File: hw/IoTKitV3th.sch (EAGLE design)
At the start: 28 parts, among them J1 4P-2.0, J2 4P-2.0, J3 4P-2.0, J4 4p-2.54

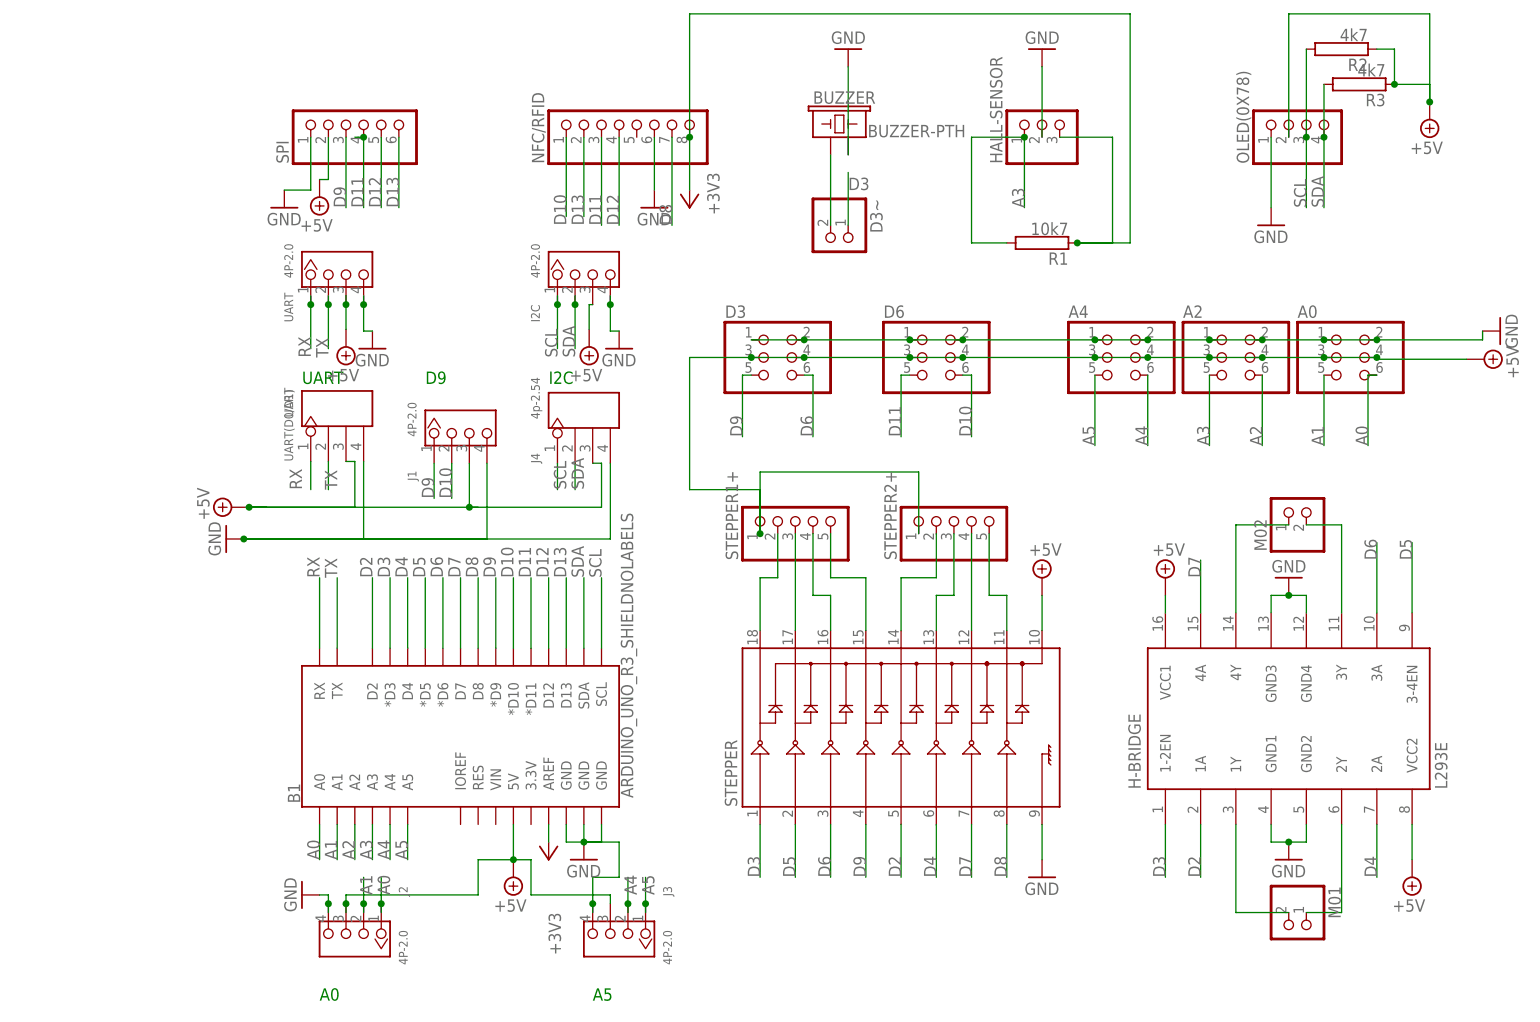
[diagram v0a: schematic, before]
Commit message: V1.1 inkl. SD Card, Poti, ESP8266, Schrift gekehrt
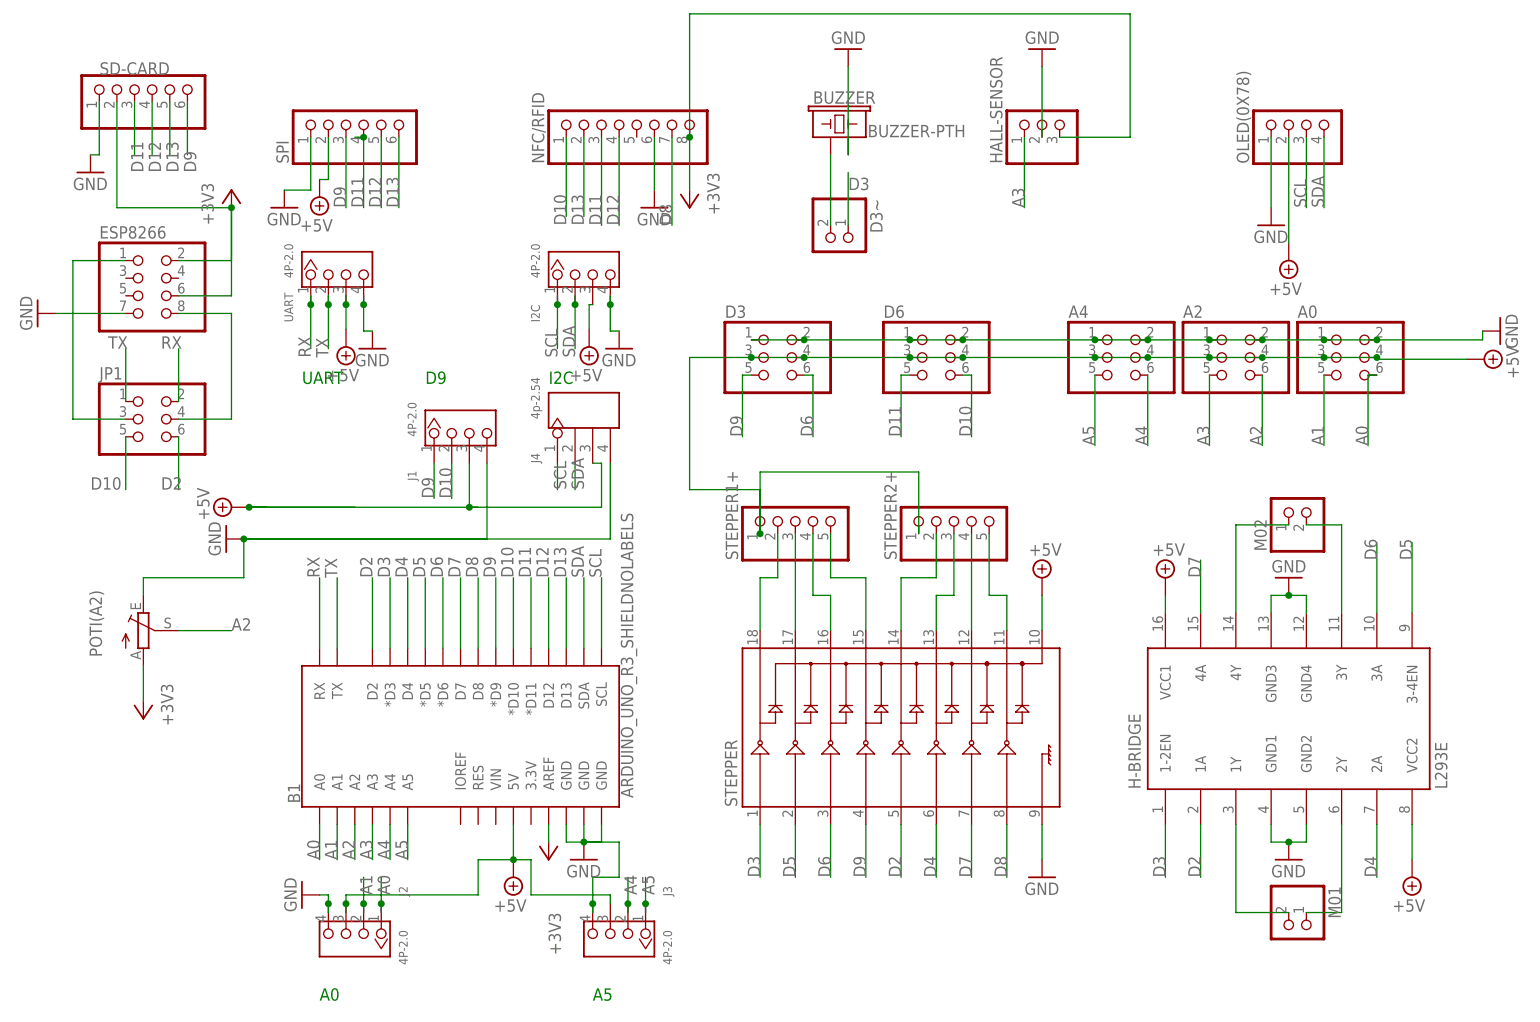
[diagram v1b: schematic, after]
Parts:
- removed R1: 10k7, resistor-power:RCA0001
- removed R2, R3: 4k7, resistor-power:RCA0001
- removed UART(D0/D1): UART, Seeed-Connector:DIP-BLACK-MALE-HEADER-VERT(4P-2.54)
- added ESP8266: (no value), pinhead:PINHD-2X4
- added JP1: (no value), pinhead:PINHD-2X3
- added POTI(A2): (no value), pot:TRIM_EU-B25P
- added SD-CARD: (no value), pinhead:PINHD-1X6
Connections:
- new net N$8: ESP8266.1, JP1.3
- new net N$9: ESP8266.8, JP1.4
- net +3V3: now also ESP8266.2, ESP8266.6, POTI(A2).A, SD-CARD.2; no longer R1.1
- net +5V: no longer R2.1, R3.1, UART(D0/D1).P$3
- net A2: now also POTI(A2).S
- net A3: no longer R1.2
- net D10: now also JP1.5
- net D11: now also SD-CARD.3
- net D12: now also SD-CARD.4
- net D13: now also SD-CARD.5
- net D2: now also JP1.6
- net D9: now also SD-CARD.6
- net GND: now also ESP8266.7, POTI(A2).E, SD-CARD.1; no longer UART(D0/D1).P$4
- net RX: now also JP1.2; no longer UART(D0/D1).P$1
- net SCL: no longer R2.2
- net SDA: no longer R3.2
- net TX: now also JP1.1; no longer UART(D0/D1).P$2

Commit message: Korrektur SD Karten belegung
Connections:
- net D11: now also SD-CARD.4; no longer SD-CARD.3
- net D12: now also SD-CARD.3; no longer SD-CARD.4
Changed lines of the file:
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@@
 </segment>
 <segment>
-<pinref part="SD-CARD" gate="A" pin="3"/>
-<wire x1="-21.59" y1="129.54" x2="-21.59" y2="121.92" width="0.1524" layer="91"/>
-<label x="-20.32" y="119.38" size="1.778" layer="95" rot="R90"/>
+<pinref part="SD-CARD" gate="A" pin="4"/>
+<wire x1="-19.05" y1="129.54" x2="-19.05" y2="121.92" width="0.1524" layer="91"/>
+<label x="-17.78" y="119.38" size="1.778" layer="95" rot="R90"/>
 </segment>
 </net>
@@
 </segment>
 <segment>
-<pinref part="SD-CARD" gate="A" pin="4"/>
-<wire x1="-19.05" y1="129.54" x2="-19.05" y2="121.92" width="0.1524" layer="91"/>
-<label x="-17.78" y="119.38" size="1.778" layer="95" rot="R90"/>
+<pinref part="SD-CARD" gate="A" pin="3"/>
+<wire x1="-21.59" y1="129.54" x2="-21.59" y2="121.92" width="0.1524" layer="91"/>
+<label x="-20.32" y="119.38" size="1.778" layer="95" rot="R90"/>
 </segment>
 </net>
